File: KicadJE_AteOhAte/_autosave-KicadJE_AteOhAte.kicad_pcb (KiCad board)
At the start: 2 copper layers, 100 x 100 mm, 201 parts, among them J201 In_Accent, J202 In Gate, J203 Out Tom, J301 PJRAS2X2S01AUX, J302 Conn_01x03, P201 Doepfer_Power_10pin, Q201 MMBT2222A, Q202 MMBT2222A, Q203 MMBT2222A, Q204 MMBT2222A, Q205 MMBT2907A, Q206 MMBT2222A, Q207 MMBT2222A, SW201 Con/Tom, U201 TL072, U202 TL072, U203 TL072, U301 TL072, U302 TL072, U303 TL072

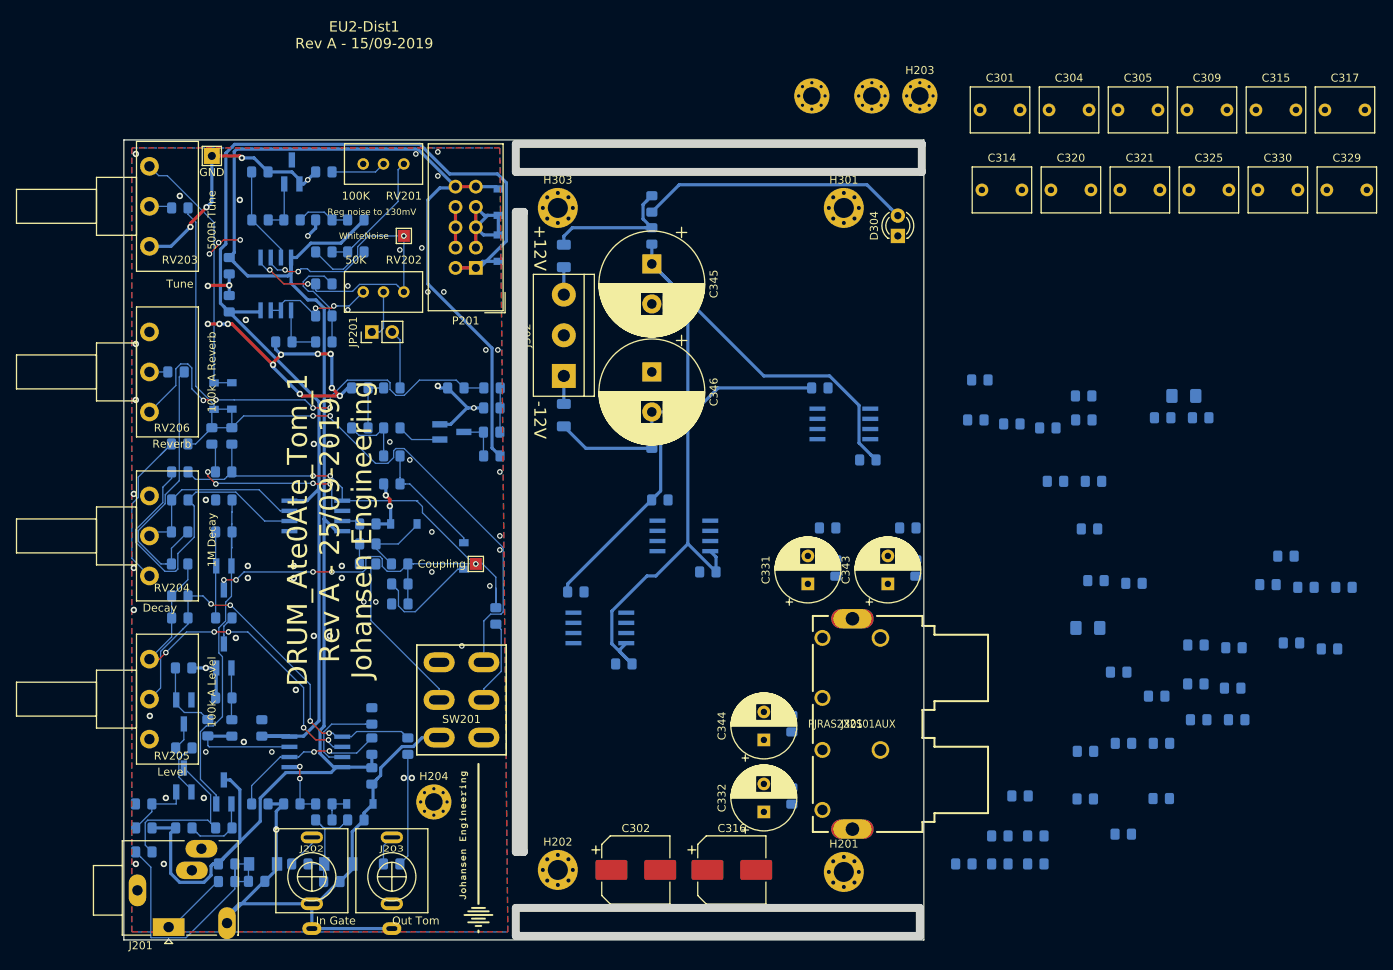
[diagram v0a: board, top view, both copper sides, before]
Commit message: SCH Error in RIAA fixed (link C313 327 area)
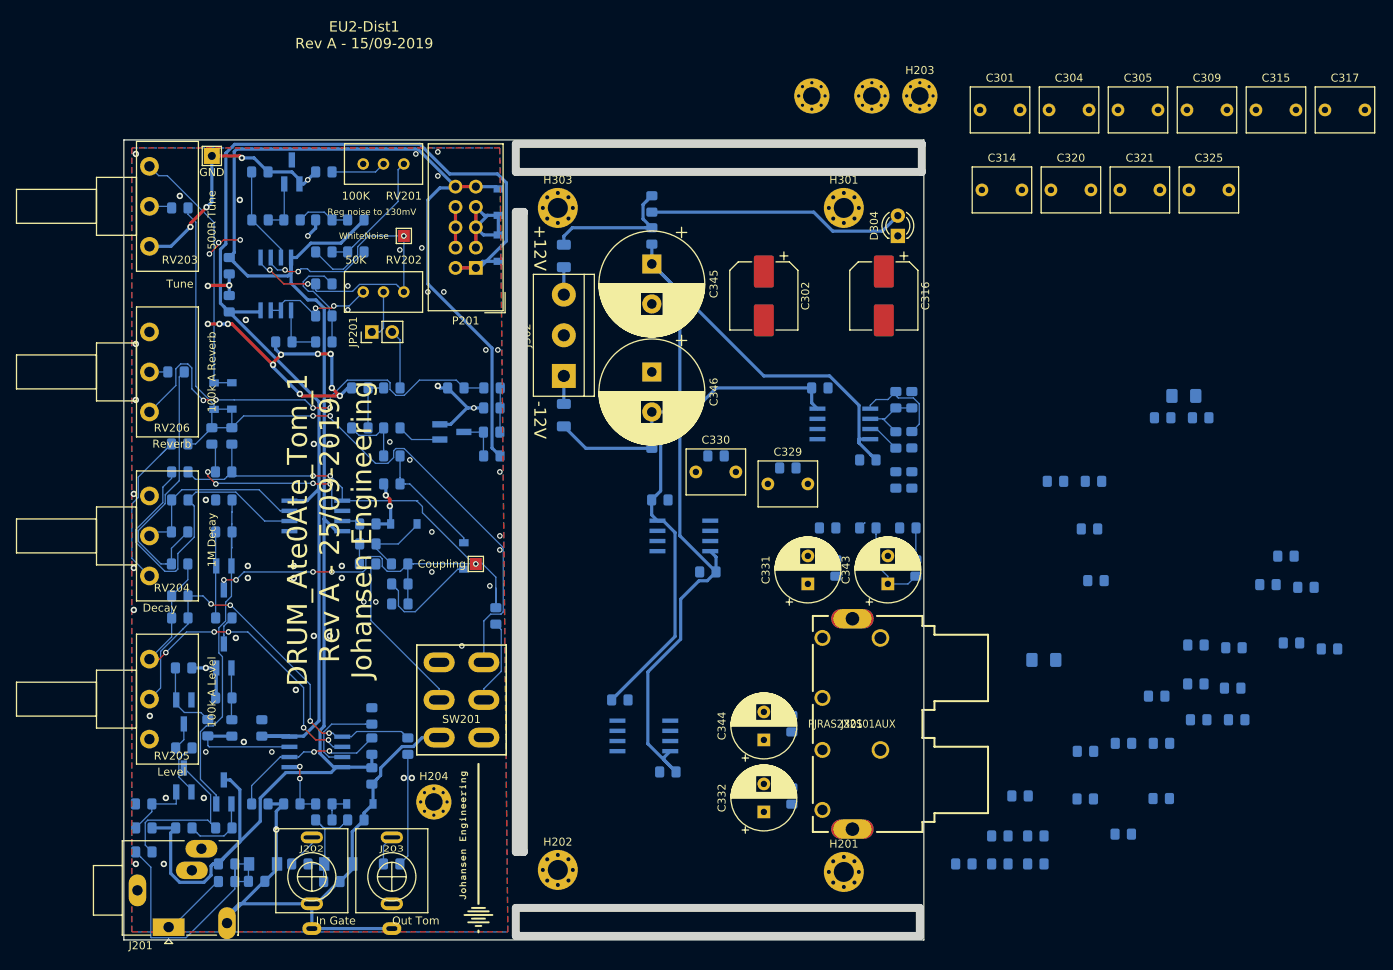
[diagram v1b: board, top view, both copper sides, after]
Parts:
- moved C329 78.9 mm to (130.5, 93.0)
- moved C330 78.6 mm to (121.5, 91.5)
- moved C316 74.2 mm to (145.0, 69.5), turned to 270 degrees
- moved C302 73.5 mm to (130.0, 69.5), turned to 270 degrees
- moved R315 59.0 mm to (146.5, 87.5), turned to 90 degrees
- moved C328 54.6 mm to (124.0, 89.5)
- moved C327 48.6 mm to (133.0, 91.0)
- moved R317 31.6 mm to (143.0, 98.5)
- moved R321 24.7 mm to (146.5, 92.5), turned to 90 degrees
- moved C322 18.2 mm to (148.5, 92.5), turned to 270 degrees
- moved C336 14.6 mm to (118.0, 129.0)
- moved C338 14.6 mm to (112.0, 120.0)
- moved U303 14.6 mm to (115.0, 124.5)
- moved R318 12.7 mm to (148.5, 87.5), turned to 270 degrees
- moved C318 10.3 mm to (146.5, 82.5), turned to 90 degrees
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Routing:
- net -12V: track 203.8 -> 220.8 mm
- net Net-(C318-Pad2): track 0.00 -> 12.3 mm
- net +12V: track 350.5 -> 362.3 mm
- net In_R: track 0.00 -> 11.5 mm
- net Net-(C318-Pad1): track 0.00 -> 8.54 mm
- net R_GainOut: track 0.00 -> 4.19 mm
- net Net-(C341-Pad1): track 0.00 -> 3.99 mm
- net Net-(D304-Pad2): track 33.8 -> 32.5 mm
- net Net-(C322-Pad1): track 0.00 -> 0.95 mm
